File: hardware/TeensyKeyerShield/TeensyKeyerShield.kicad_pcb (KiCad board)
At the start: 2 copper layers, 102 parts, among them J1 Conn_01x02, J10 Conn_01x04, J11 Conn_02x06_Counter_Clockwise, J12 AudioJack3_SwitchTR, J13 Conn_02x06_Counter_Clockwise, J14 Conn_01x04, J2 Conn_01x02, J3 Conn_01x02, J4 Conn_01x02, J5 AudioJack3_SwitchTR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

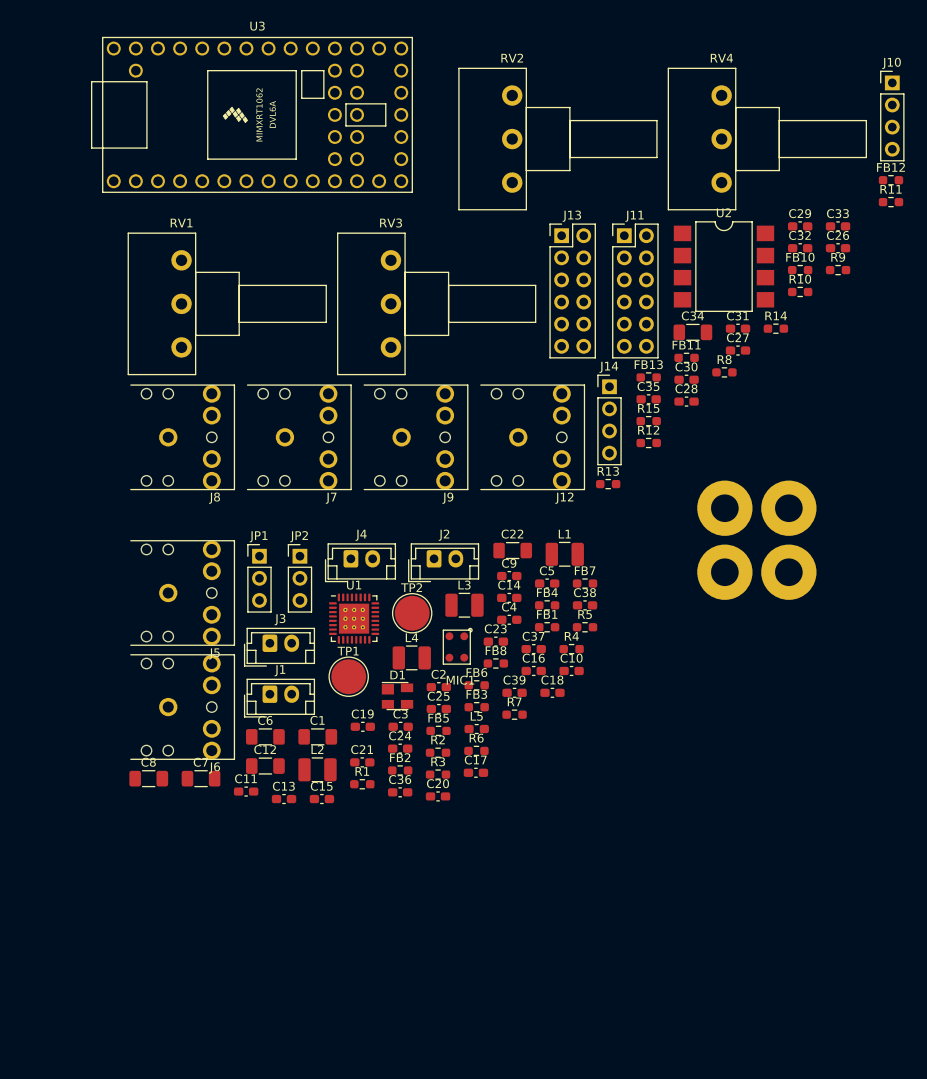
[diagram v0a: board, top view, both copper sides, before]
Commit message: TeensyKeyerShield floorplanning
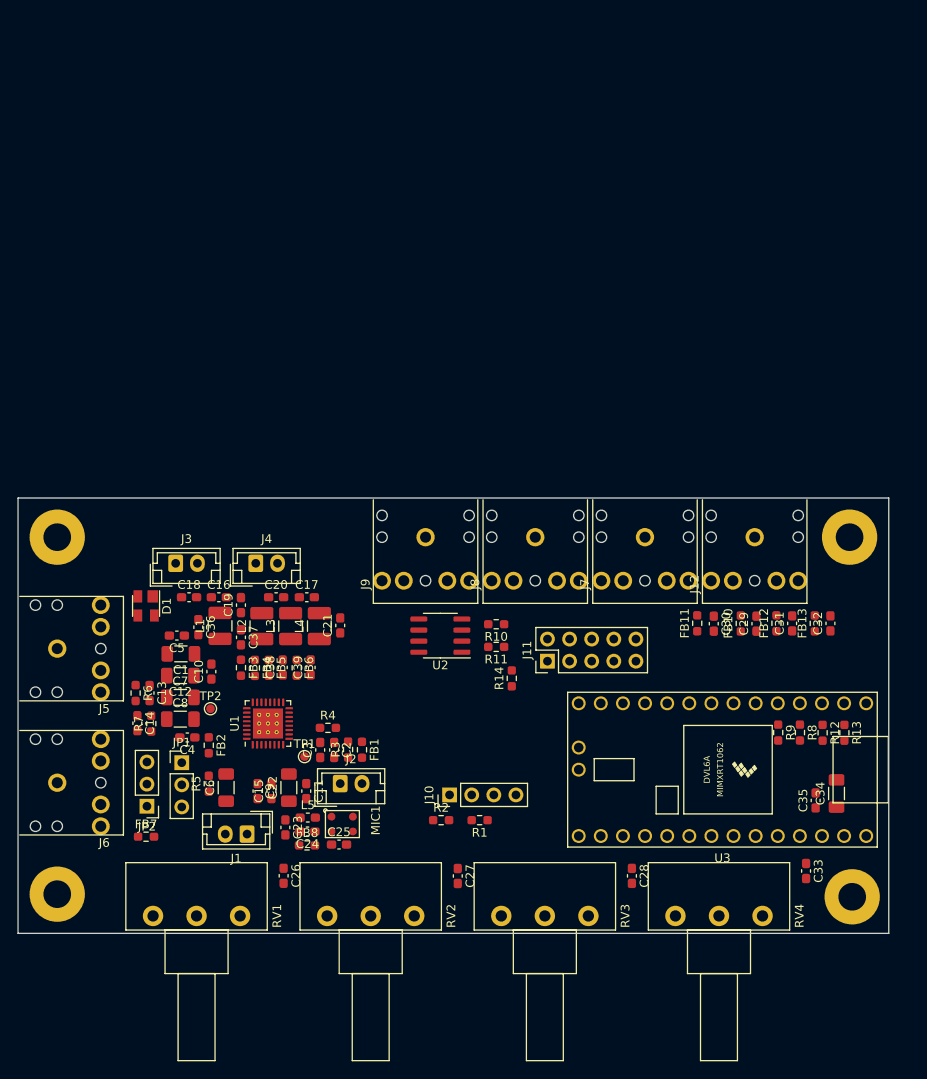
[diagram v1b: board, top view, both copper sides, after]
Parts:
- removed J13: Conn_02x06_Counter_Clockwise, Connector_PinHeader_2.54mm:PinHeader_2x06_P2.54mm_Vertical
- removed J14: Conn_01x04, Connector_PinHeader_2.54mm:PinHeader_1x04_P2.54mm_Vertical
- removed R15: 4.7K, Resistor_SMD:R_0603_1608Metric_Pad0.98x0.95mm_HandSolder
- J11: value Conn_02x06_Counter_Clockwise -> Conn_02x05_Odd_Even; footprint Connector_PinHeader_2.54mm:PinHeader_2x06_P2.54mm_Vertical -> Connector_PinHeader_2.54mm:PinHeader_2x05_P2.54mm_Vertical
- R14: value 4.7K -> 470
- TP1, TP2: footprint TestPoint:TestPoint_Pad_D4.0mm -> TestPoint:TestPoint_Pad_D1.0mm
- U2: value LTV-827S -> MOCD217R2M; footprint Package_DIP:SMDIP-8_W9.53mm -> Package_SO:SOIC-8_3.9x4.9mm_P1.27mm
- moved J10 96.3 mm to (129.6, 104.1), turned to 90 degrees
- moved C26 96.2 mm to (110.5, 113.4), turned to 270 degrees
- moved U3 92.2 mm to (160.9, 101.2), turned to 180 degrees
- moved MH4 91.8 mm to (84.5, 115.5)
- moved RV2 86.9 mm to (115.5, 118.0), turned to 270 degrees
- moved RV4 84.4 mm to (155.5, 118.0), turned to 270 degrees
- moved MH3 84.1 mm to (84.5, 74.5)
- moved C33 74.1 mm to (170.5, 112.8), turned to 270 degrees
- moved C27 68.4 mm to (130.5, 113.4), turned to 270 degrees
- moved R11 68.3 mm to (134.9, 87.1), turned to 180 degrees
- moved RV3 66.5 mm to (135.5, 118.0), turned to 270 degrees
- moved RV1 65.4 mm to (95.5, 118.0), turned to 270 degrees
- moved FB7 58.2 mm to (94.7, 108.9)
- moved C34 55.5 mm to (174.0, 103.9), turned to 90 degrees
- moved C28 54.8 mm to (150.5, 113.4), turned to 270 degrees
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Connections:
- J11 pad 2: Net-(J11-Pad2) -> GND
- J11 pad 6: Net-(J11-Pad6) -> +3V3
- J11 pad 7: GND -> Net-(J11-Pad7)
- J11 pad 8: GND -> Net-(J11-Pad8)
- J11 pad 9: GND -> Net-(J11-Pad9)
- R14 pad 1: Net-(J14-Pad1) -> Net-(R14-Pad1)
- R14 pad 2: +3V3 -> Net-(J11-Pad4)
- U2 pad 1: Net-(R10-Pad2) -> Net-(R11-Pad2)
- U2 pad 3: Net-(R11-Pad2) -> Net-(R10-Pad2)
- U2 pad 6: Net-(J9-PadT) -> Net-(J9-PadR)
- U2 pad 8: Net-(J9-PadR) -> Net-(J9-PadT)
- U3 pad 11: Net-(J11-Pad1) -> Net-(J11-Pad7)
- U3 pad 12: Net-(J11-Pad2) -> Net-(J11-Pad5)
- U3 pad 13: Net-(J11-Pad3) -> Net-(J11-Pad9)
- U3 pad 14: Net-(J11-Pad4) -> Net-(J11-Pad3)
- U3 pad 2: Net-(C31-Pad1) -> Net-(C32-Pad1)
- U3 pad 20: Net-(J11-Pad5) -> Net-(J11-Pad1)
- U3 pad 21: Net-(J11-Pad6) -> Net-(R14-Pad1)
- U3 pad 3: Net-(C32-Pad1) -> Net-(C31-Pad1)
- U3 pad 7: EXTMEM2 -> Net-(J11-Pad8)
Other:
- board outline added: 100 x 50 mm

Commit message: Updated with some routing
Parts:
- moved TP2 1.20 mm to (102.1, 95.4)
- moved TP1 0.51 mm to (112.4, 99.6)
- moved C25 0.10 mm to (116.9, 109.9)
- turned C30 to 90 degrees
- turned R6 to 90 degrees
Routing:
- net GND: track 0.00 -> 67.6 mm, vias 0 -> 25
- net Net-(R10-Pad1): track 0.00 -> 36.7 mm
- net Net-(FB11-Pad2): track 0.00 -> 28.2 mm
- net Net-(J9-PadS): track 0.00 -> 25.3 mm
- net +5V: track 0.00 -> 21.3 mm, vias 0 -> 3
- net Net-(FB10-Pad2): track 0.00 -> 21.0 mm
- net +3V3: track 0.00 -> 17.4 mm, vias 0 -> 4
- net MICPTT: track 0.00 -> 16.6 mm
- net Net-(R11-Pad1): track 0.00 -> 16.0 mm
- net Net-(C29-Pad1): track 0.00 -> 14.6 mm
- net JACKDET: track 0.00 -> 14.2 mm, vias 0 -> 2
- net Net-(C31-Pad1): track 0.00 -> 14.1 mm
- net Net-(C15-Pad1): track 0.00 -> 13.7 mm
- net Net-(C32-Pad1): track 0.00 -> 13.3 mm
- net Net-(C2-Pad1): track 0.00 -> 12.8 mm
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
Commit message: Most routing done
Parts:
- removed JP2: Jumper_3_Open, Connector_PinHeader_2.54mm:PinHeader_1x03_P2.54mm_Vertical
- J10: footprint Connector_PinHeader_2.54mm:PinHeader_1x04_P2.54mm_Vertical -> Connector_JST:JST_PH_B4B-PH-K_1x04_P2.00mm_Vertical
- JP1: value Jumper_3_Open -> Conn_02x03_Odd_Even; footprint Connector_PinHeader_2.54mm:PinHeader_1x03_P2.54mm_Vertical -> Connector_PinHeader_2.54mm:PinHeader_2x03_P2.54mm_Vertical
- moved J10 6.34 mm to (135.9, 104.0), turned to 180 degrees
- moved R2 4.40 mm to (133.0, 107.2)
- moved R1 3.78 mm to (136.8, 107.2)
- moved JP1 3.54 mm to (95.3, 100.9)
- moved C33 1.15 mm to (171.3, 112.0), turned to 0 degrees
- moved FB7 0.91 mm to (94.6, 109.8)
- moved D1 0.45 mm to (94.5, 82.8)
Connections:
- D1 pad 2: Net-(C15-Pad1) -> Net-(C13-Pad1)
- D1 pad 3: Net-(C13-Pad1) -> Net-(C14-Pad1)
- D1 pad 4: Net-(C14-Pad1) -> Net-(C15-Pad1)
- J10 pad 1: SDIN -> SCLK
- J10 pad 2: SCLK -> SDIN
- JP1 pad 2: Net-(C15-Pad1) -> Net-(J6-PadR)
- JP1 pad 3: Net-(J6-PadT) -> Net-(FB7-Pad1)
- U3 pad 7: Net-(J11-Pad8) -> Net-(R11-Pad1)
- U3 pad 8: Net-(R11-Pad1) -> Net-(J11-Pad8)
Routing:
- net +3V3: track 17.4 -> 231.9 mm, vias 4 -> 8
- net +5V: track 21.3 -> 162.9 mm
- net MICPTT: track 16.6 -> 105.3 mm, vias 0 -> 1
- net SCLK: track 5.24 -> 68.0 mm, vias 0 -> 1
- net MCLK: track 0.00 -> 61.9 mm
- net BCLK: track 4.01 -> 65.5 mm, vias 0 -> 2
- net SDIN: track 6.07 -> 66.9 mm, vias 0 -> 1
- net LRCLK: track 7.28 -> 66.8 mm, vias 0 -> 2
- net Net-(C26-Pad1): track 0.00 -> 55.1 mm
- net DACDAT: track 1.57 -> 49.7 mm, vias 1 -> 2
- net ADCDAT: track 4.38 -> 45.9 mm
- net Net-(C27-Pad1): track 0.00 -> 37.8 mm
- net JACKDET: track 14.2 -> 49.9 mm
- net Net-(C15-Pad1): track 13.7 -> 40.8 mm, vias 0 -> 1
- net Net-(R14-Pad1): track 0.00 -> 24.3 mm, vias 0 -> 1
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- added copper zone on B.Cu, net GND
- added copper zone on F.Cu, net GND

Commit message: Mostly done with routing and silkscreen
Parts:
- added G***: OSHW-logo_silkscreen-front_2mm, TeensyKeyerShield:OSHW-logo_silkscreen-front_2mm, F.Cu at (94.5, 72.9)
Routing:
- net GND: track 89.8 -> 105.6 mm, vias 29 -> 30
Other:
- outline, holes or cut-outs redrawn
- board text added: "CW Keyer Shield © 2021 SofterHardware"

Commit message: Added ibom.html
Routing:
- net GND: track 105.6 -> 310.2 mm, vias 30 -> 72
- net Net-(C26-Pad1): track 55.1 -> 55.6 mm
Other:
- board text added: "CW Keyer Shield 0.9 © 2021 SofterHardware"
- board text added: "Headphones"
- board text added: "I2C"
- board text added: "Key/PTT Out"
- board text added: "LIN"
- board text added: "LSPKR"
- board text added: "Microphone"
- board text added: "PTT In"
- board text added: "Paddle"
- board text added: "RIN"
- board text added: "RSPKR"
- board text added: "Sidetone Pitch"
- board text added: "Sidetone Volume"
- board text added: "Speed"
- board text added: "Straight Key"
- board text added: "Teensy 4.0"
- board text added: "Volume"
- board text removed: "CW Keyer Shield © 2021 SofterHardware"
